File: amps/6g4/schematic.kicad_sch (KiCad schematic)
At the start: 77 parts, among them T1 8087, T2 45216

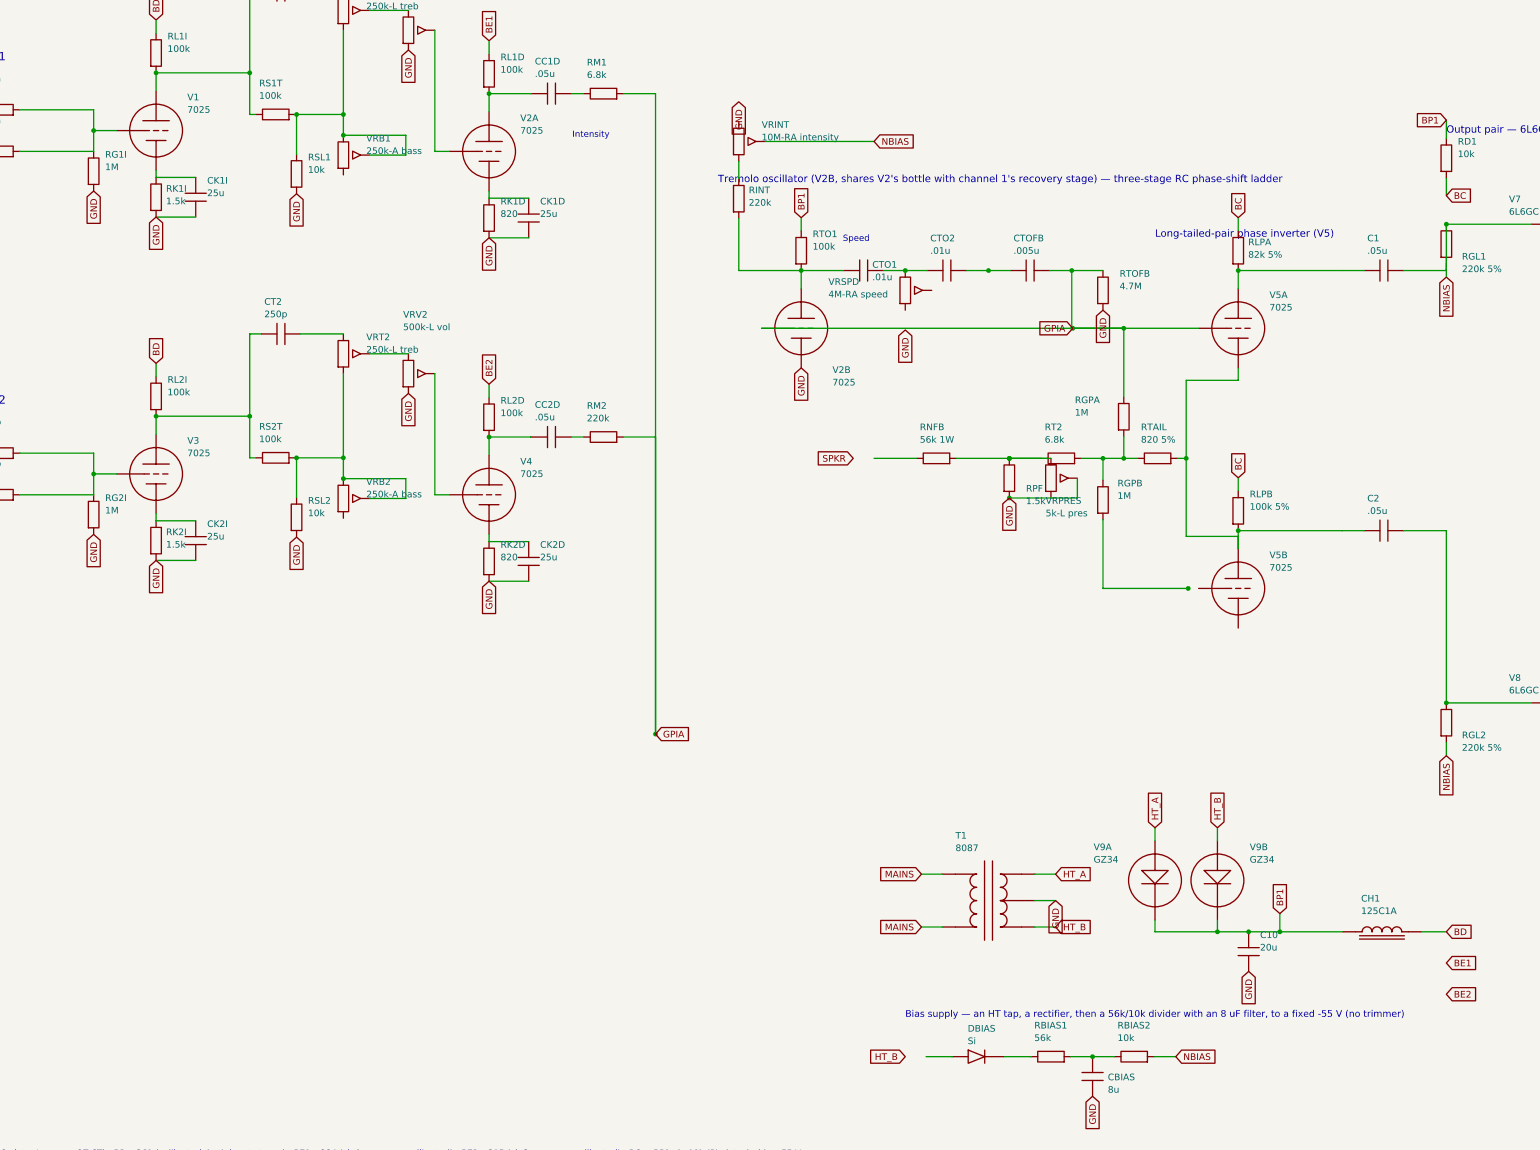
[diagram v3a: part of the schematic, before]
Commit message: Fix: deterministic schematic ids and wires split at every join
- _u() is uuid5 over (amp id, emission order), so a regeneration of an
  unchanged script is byte-identical and a drift gate becomes possible
- write() splits wire segments at symbol pins, wire ends and junction dots,
  so the file connects exactly what the drawing shows under KiCad's
  endpoint-only semantics (270 pins were on a wire's interior; net
  partitions unchanged on all 38 sheets)
- all sheets regenerated; aa864-bassman title block was stale (draft) and
  now matches meta.yaml (verified)

Co-Authored-By: Claude Fable 5.1 <noreply@anthropic.com>
Claude-Session: https://claude.ai/code/session_01KBMfdh37HmCL2iWcBiL5J1
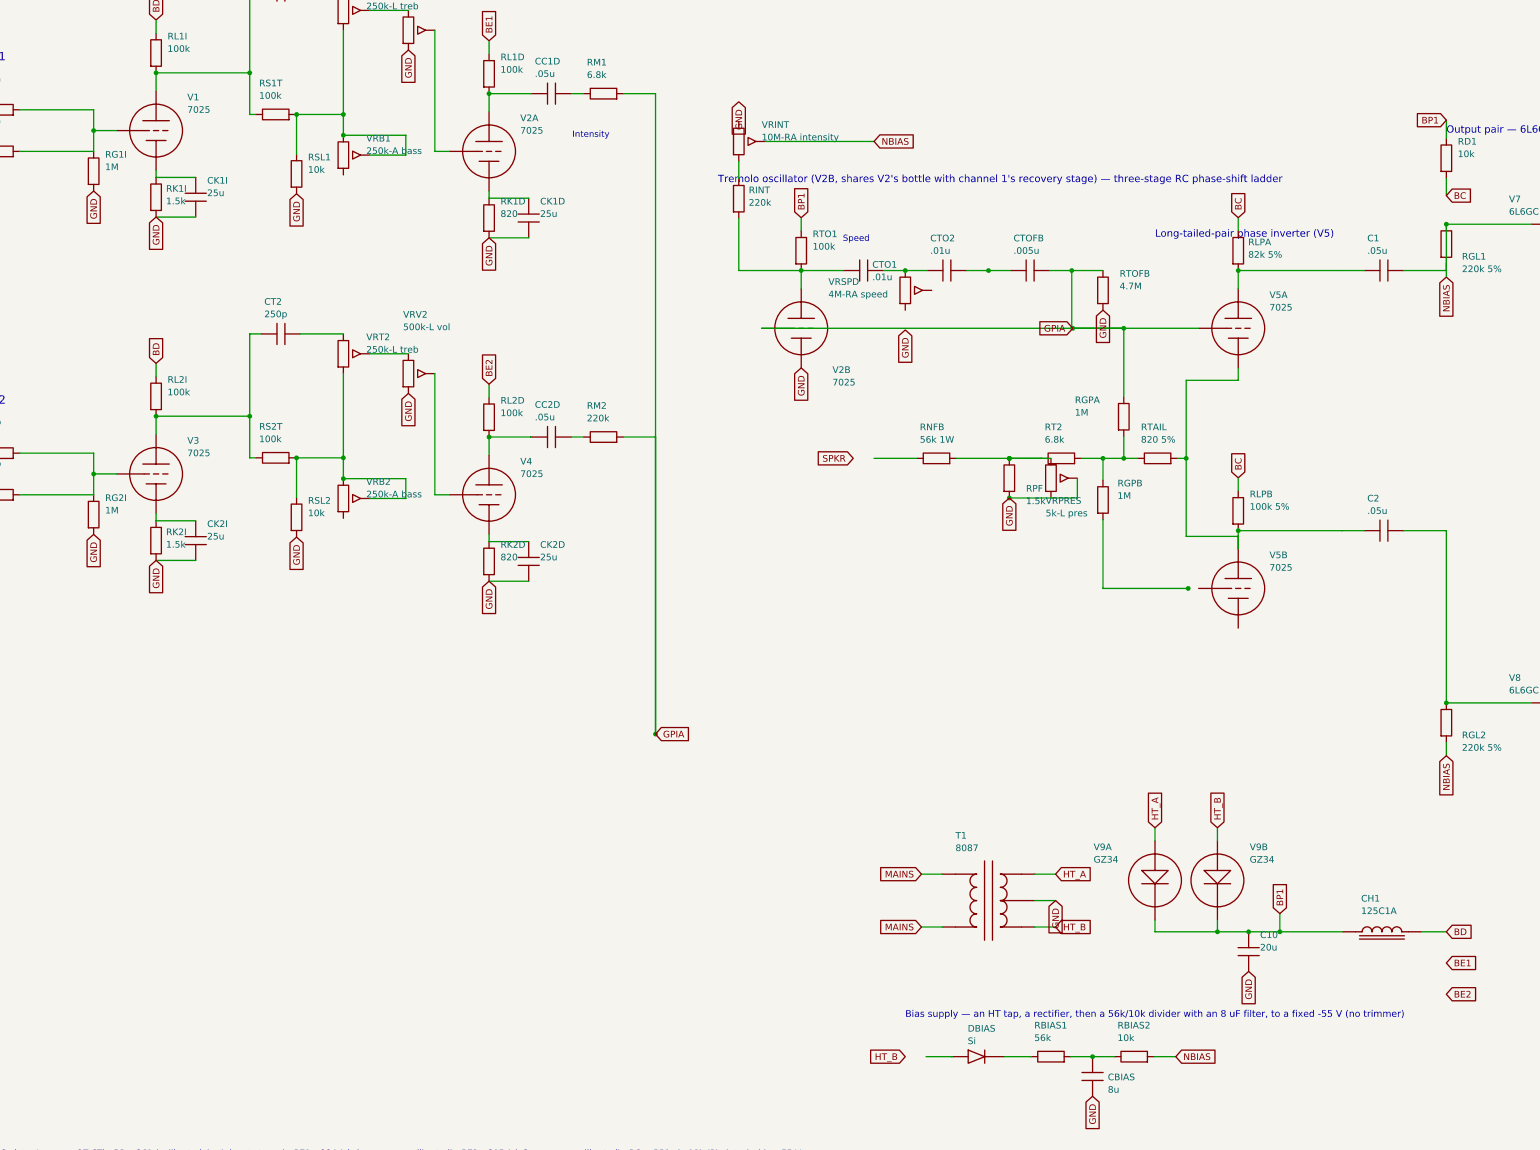
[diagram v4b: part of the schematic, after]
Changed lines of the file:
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@@
   (wire (pts (xy 35.146 50.699) (xy 49.336 50.699))
     (stroke (width 0) (type default)))
-  (wire (pts (xy 49.336 42.699) (xy 49.336 50.699))
+  (wire (pts (xy 49.336 42.699) (xy 49.336 46.699))
+    (stroke (width 0) (type default)))
+  (wire (pts (xy 49.336 46.699) (xy 49.336 50.699))
     (stroke (width 0) (type default)))
   (junction (at 49.336 46.699) (diameter 0) (color 0 0 0 0))
@@
   (wire (pts (xy 151.146 39.599) (xy 157.336 39.599))
     (stroke (width 0) (type default)))
-  (wire (pts (xy 157.336 39.599) (xy 157.336 162.699))
+  (wire (pts (xy 157.336 39.599) (xy 157.336 105.599))
+    (stroke (width 0) (type default)))
+  (wire (pts (xy 157.336 105.599) (xy 157.336 162.699))
     (stroke (width 0) (type default)))
   (text "Channel 2" (at 21.336 98.699 0)
@@
   (wire (pts (xy 35.146 116.699) (xy 49.336 116.699))
     (stroke (width 0) (type default)))
-  (wire (pts (xy 49.336 108.699) (xy 49.336 116.699))
+  (wire (pts (xy 49.336 108.699) (xy 49.336 112.699))
+    (stroke (width 0) (type default)))
+  (wire (pts (xy 49.336 112.699) (xy 49.336 116.699))
     (stroke (width 0) (type default)))
   (junction (at 49.336 112.699) (diameter 0) (color 0 0 0 0))
@@
   (global_label "GPIA" (shape input) (at 237.526 84.699 180)
     (effects (font (size 1.27 1.27)) (justify right)))
-  (wire (pts (xy 237.526 84.699) (xy 261.716 84.699))
+  (wire (pts (xy 237.526 84.699) (xy 247.336 84.699))
+    (stroke (width 0) (type default)))
+  (wire (pts (xy 247.336 84.699) (xy 261.716 84.699))
     (stroke (width 0) (type default)))
   (symbol (lib_id "cx:TRIODE") (at 269.336 84.699 0) (unit 1)
@@
   (global_label "BC" (shape input) (at 269.336 63.439 90)
     (effects (font (size 1.27 1.27)) (justify left)))
-  (wire (pts (xy 269.336 127.079) (xy 269.336 123.599))
+  (wire (pts (xy 269.336 127.079) (xy 269.336 124.699))
+    (stroke (width 0) (type default)))
+  (wire (pts (xy 269.336 124.699) (xy 269.336 123.599))
     (stroke (width 0) (type default)))
   (symbol (lib_id "cx:R") (at 269.336 119.789 0) (unit 1)
@@
   (wire (pts (xy 269.336 124.699) (xy 259.336 124.699))
     (stroke (width 0) (type default)))
-  (wire (pts (xy 259.336 94.699) (xy 259.336 124.699))
+  (wire (pts (xy 259.336 94.699) (xy 259.336 109.699))
+    (stroke (width 0) (type default)))
+  (wire (pts (xy 259.336 109.699) (xy 259.336 124.699))
     (stroke (width 0) (type default)))
   (junction (at 259.336 109.699) (diameter 0) (color 0 0 0 0))
@@
     (property "Reference" "RT2" (at 232.136 103.699 270) (effects (font (size 1.27 1.27)) (justify left)))
     (property "Value" "6.8k" (at 232.136 106.099 270) (effects (font (size 1.27 1.27)) (justify left))))
-  (wire (pts (xy 239.146 109.699) (xy 247.336 109.699))
+  (wire (pts (xy 239.146 109.699) (xy 243.336 109.699))
+    (stroke (width 0) (type default)))
+  (wire (pts (xy 243.336 109.699) (xy 247.336 109.699))
     (stroke (width 0) (type default)))
   (wire (pts (xy 231.526 109.699) (xy 225.336 109.699))
@@
     (property "Reference" "VRPRES" (at 232.32 117.849 0) (effects (font (size 1.27 1.27)) (justify left)))
     (property "Value" "5k-L pres" (at 232.32 120.249 0) (effects (font (size 1.27 1.27)) (justify left))))
-  (wire (pts (xy 233.336 109.699) (xy 225.336 109.699))
+  (wire (pts (xy 233.336 109.699) (xy 231.526 109.699))
+    (stroke (width 0) (type default)))
+  (wire (pts (xy 231.526 109.699) (xy 225.336 109.699))
     (stroke (width 0) (type default)))
   (junction (at 225.336 109.699) (diameter 0) (color 0 0 0 0))
@@
   (wire (pts (xy 301.146 73.599) (xy 309.336 73.599))
     (stroke (width 0) (type default)))
-  (wire (pts (xy 309.336 73.599) (xy 309.336 64.699))
+  (wire (pts (xy 309.336 73.599) (xy 309.336 72.319))
+    (stroke (width 0) (type default)))
+  (wire (pts (xy 309.336 72.319) (xy 309.336 64.699))
     (stroke (width 0) (type default)))
   (symbol (lib_id "cx:C") (at 297.336 123.599 90) (unit 1)
@@
     (property "Reference" "RGL1" (at 312.336 70.909 0) (effects (font (size 1.27 1.27)) (justify left)))
     (property "Value" "220k 5%" (at 312.336 73.309 0) (effects (font (size 1.27 1.27)) (justify left))))
-  (wire (pts (xy 309.336 72.319) (xy 309.336 74.859))
+  (wire (pts (xy 309.336 72.319) (xy 309.336 73.599))
+    (stroke (width 0) (type default)))
+  (wire (pts (xy 309.336 73.599) (xy 309.336 74.859))
     (stroke (width 0) (type default)))
   (global_label "NBIAS" (shape input) (at 309.336 74.859 270)
@@
   (wire (pts (xy 265.336 198.439) (xy 265.336 200.699))
     (stroke (width 0) (type default)))
-  (wire (pts (xy 253.336 200.699) (xy 277.336 200.699))
+  (wire (pts (xy 253.336 200.699) (xy 265.336 200.699))
+    (stroke (width 0) (type default)))
+  (wire (pts (xy 265.336 200.699) (xy 271.336 200.699))
+    (stroke (width 0) (type default)))
+  (wire (pts (xy 271.336 200.699) (xy 277.336 200.699))
     (stroke (width 0) (type default)))
   (junction (at 265.336 200.699) (diameter 0) (color 0 0 0 0))
@@
   (global_label "HT_B" (shape input) (at 205.336 224.699 180)
     (effects (font (size 1.27 1.27)) (justify right)))
-  (wire (pts (xy 209.336 224.699) (xy 214.416 224.699))
+  (wire (pts (xy 209.336 224.699) (xy 214.256 224.699))
+    (stroke (width 0) (type default)))
+  (wire (pts (xy 214.256 224.699) (xy 214.416 224.699))
     (stroke (width 0) (type default)))
   (symbol (lib_id "cx:DIODE_SS") (at 219.336 224.699 0) (unit 1)

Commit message: Fix: schematic wiring on 6g3, 6g4, 6g5, 6g6b
- long-tailed pair tail moved off section B's plate to its cathode (6g3,
  6g4, 6g5); 6g4 V8 plate lead was drawn under its grounded cathode
- 6g6b: all five OT leads on bare coordinates with the secondary drawn on
  the primary side; bias line taken off the bleeder's grounded end (NBIAS
  and GND one net); both tone networks rebuilt; mixing bus ran through
  V3A's bottle
- eight parts shorted end to end, invisible to the pin check: 6g4 RGL1;
  6g5 RG5 (mixing node on ground); 6g6b C11, RG4B, RNFB, RTAIL, RTN1, VR3
- 6g5: treble pot runs off each other's lug, driver run 12 mm short of
  V6A grid, CFB1 rotated but wired upright, choke leads short both ends
- five dated waivers (bridge rectifier centre tap, footswitch terminal
  not lettered on the source, mains side outside the drawing, VR7's
  undesignated cap)
- OPEN, not guessed: 6g5 presence network is drawn as a DC path to ground
  (RPRES + pot in series) while netlist.cir has RT2 to ground and calls the
  network DC-neutral; sources do not settle it — sheet stays unclaimed

Co-Authored-By: Claude Fable 5.1 <noreply@anthropic.com>
Claude-Session: https://claude.ai/code/session_01KBMfdh37HmCL2iWcBiL5J1
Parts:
- removed C1: .05u, symbol cx:C
- removed CTO2: .01u, symbol cx:C
- removed RBIAS1: 56k, symbol cx:R
- removed RGL1, RGL2: 220k 5%, symbol cx:R
- removed RLPA: 82k 5%, symbol cx:R
- removed RT2: 6.8k, symbol cx:R
- removed RTOFB: 4.7M, symbol cx:R
- added C2: .05u, symbol cx:C
- added CBIAS: 8u, symbol cx:C
- added CTOFB: .005u, symbol cx:C
- added RINT: 220k, symbol cx:R
- added RLPB: 100k 5%, symbol cx:R
- added RNFB: 56k 1W, symbol cx:R
- added RS1: 470 1W, symbol cx:R
- added T2: 45216, symbol cx:OT_PP
- CTO2: renamed from CTOFB; value .005u -> .01u
- RBIAS1: renamed from CBIAS; value 8u -> 56k; symbol cx:C -> cx:R
- RGL1: renamed from RS1; value 470 1W -> 220k 5%
- RGL2: renamed from RS2; value 470 1W -> 220k 5%
- RLPA: renamed from RLPB; value 100k 5% -> 82k 5%
- RS2: renamed from T2; value 45216 -> 470 1W; symbol cx:OT_PP -> cx:R
- RT2: renamed from RNFB; value 56k 1W -> 6.8k
- RTOFB: renamed from RINT; value 220k -> 4.7M
- renumbered C2 to C1
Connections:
- net BC: now also RLPB.1
- net BP1: now also RS2.2, RS1.2, T2.2 (CT); no longer RGL1.2, RGL2.2
- net CH1 IN 1: now also R1a.1
- net CH1 IN 2: now also R2a.1
- net CH2 IN 1: now also R1b.1
- net CH2 IN 2: now also R2b.1
- net GND: now also RTOFB.2, VRINT.1, VRSPD.2 (W), VRSPD.3, CBIAS.2, T2.5 (SEC_C); no longer RBIAS1.2, RS2.5 (SEC_C)
- net HT_B: now also DBIAS.1 (A)
- net NBIAS: now also RGL1.2, RGL2.2; no longer V7.2 (G1)
- net SPKR: now also RNFB.1, T2.4 (SEC_H); no longer RS2.4 (SEC_H)
- net at V5A.1 (P): now also C1.1, RLPA.2
- net at CTO2.1: now also CTO1.2, VRSPD.1
- net at CTO2.2: now also CTOFB.1; no longer V2B.2 (G)
- net at RS1T.2, VRB1.1, VRB1.2 (W)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: no longer RSL1.1
- net at VRB1.3: now also RSL1.1
- net at CTO1.1, RTO1.2, V2B.1 (P): now also RINT.2; no longer RTOFB.2
- net at RPF.1, VRPRES.1: now also RT2.1, RNFB.2; no longer RT2.2
- net at RGPA.2, RGPB.1, RTAIL.1: now also RT2.2
- net at RGL1.1: now also C1.2, V7.2 (G1); no longer V7.3 (G2)
- net at RS2T.2, VRB2.1, VRB2.2 (W)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: no longer RSL2.1
- net at DBIAS.2 (K): now also RBIAS1.1
- net at RBIAS2.1: now also RBIAS1.2, CBIAS.1; no longer RBIAS1.1
- net at V8.2 (G1): now also RGL2.1, C2.2; no longer C1.2
- net at VRINT.3: now also RINT.1; no longer RTOFB.1
- net at V7.1 (P): now also T2.1 (PRI_A); no longer RS2.1 (PRI_A)
- net at VRB2.3: now also RSL2.1
- net at V5B.2 (G): now also RGPB.2
- net at V5B.3 (K): now also RTAIL.2, V5A.3 (K)
- net at V8.3 (G2): now also RS2.1; no longer RGL2.1
- net at V8.1 (P): now also T2.3 (PRI_B)
- new net: CTOFB.2, RTOFB.1, V2B.2 (G)
- new net: RS1.1, V7.3 (G2)
- new net: C2.1, RLPB.2, V5B.1 (P)
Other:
- moved on the sheet: C1, CTO2, RGL1, RGL2, RLPA, RT2, RTOFB

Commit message: Fix: AB763 Super and 6G4 corrections read back from the factory sheets
AB763 Super (closes #15, closes #16)

The model omitted the Normal channel's second triode entirely and gave the
Vibrato second stage, mix driver and reverb recovery a cathode resistor each.
The C-FD schematic's boxed [A] and [E] are inter-stage connections: [A] ties
the Normal and Vibrato second stages to ONE 820 / 25u network, [E] ties the mix
driver and reverb recovery to another. Because our model omitted one triode's
current, this page claimed the printed chart was internally impossible at three
cathode nodes. It is not. With XV1B added and the shared nodes joined:

  KA   chart 2.1 V   was 1.5 V (-30.0%)   now 2.2 V (+3.6%)
  KE   chart 2.0 V   was 1.5 V (-27.0%)   now 2.2 V (+8.8%)
  PV2  chart 270 V   was 231 V (-14.4%)   now 277 V (+2.6%)

All 20 gated nodes now pass; the accusation is retracted in notes.md and the
retraction is recorded in meta.yaml as audit trail. This is the fourth time the
corpus has accused a factory sheet and been the one at fault.

The Middle control is 10 kOhm-A, not the 250 kOhm published -- 25x, so the
tone-stack curve was wrong, not just the label. Corrected everywhere including
the lab preset; the blackface mid-scoop returns at 15.6 dB / 419 Hz.

With the Middle pot confirmed, topology.tone_stack moves tb -> fmv: this
chassis carries a fixed bleed on one channel and a real Middle pot on the
other, and filing it as treble/bass contradicted its own parts list. The field
names the Vibrato channel and notes.md documents the mixed case.

6G4

Same presence idiom as the 6G5, read off the A-FJ sheet: a 1500 foot resistor
to ground with the 5K-L pot in series with a .1 cap paralleling it. The cap was
missing from the corpus; added as CPRES, 0.1uF, the 200 V read off the layout
page's own .1-200 lettering rather than defaulted from the notice's 400 V.

RNFB is 10 kOhm, not 56 -- traced end to end onto the OT secondary hot. RD1 is
4700 1W, not 10k: the netlist called t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
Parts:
- removed RBIAS1: 56k, symbol cx:R
- removed RGL1, RGL2: 220k 5%, symbol cx:R
- added CBIAS: 8u, symbol cx:C
- added CPRES: .1u 200V, symbol cx:C
- added RS1: 470 1W, symbol cx:R
- added T2: 45216, symbol cx:OT_PP
- RBIAS1: renamed from CBIAS; value 8u -> 56k; symbol cx:C -> cx:R
- RD1: value 10k -> 4.7k 1W
- RGL1: renamed from RS1; value 470 1W -> 220k 5%
- RGL2: renamed from RS2; value 470 1W -> 220k 5%
- RNFB: value 56k 1W -> 10k
- RS2: renamed from T2; value 45216 -> 470 1W; symbol cx:OT_PP -> cx:R
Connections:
- net BP1: now also RS1.2, T2.2 (CT); no longer RGL1.2, RGL2.2
- net GND: now also CBIAS.2, CPRES.2, T2.5 (SEC_C); no longer RBIAS1.2, RS2.5 (SEC_C), VRPRES.2 (W), VRPRES.3
- net NBIAS: now also RGL1.2, RGL2.2
- net SPKR: now also T2.4 (SEC_H); no longer RS2.4 (SEC_H)
- net at RNFB.2, RPF.1, RT2.1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: now also VRPRES.2 (W)
- net at C1.2, V7.2 (G1): now also RGL1.1
- net at V7.1 (P): now also T2.1 (PRI_A); no longer RS2.1 (PRI_A)
- net at V7.3 (G2): now also RS1.1; no longer RGL1.1
- net at RBIAS1.1: now also DBIAS.2 (K); no longer RBIAS2.1
- net at RGL2.1: now also C2.2, V8.2 (G1); no longer V8.3 (G2)
- net at V8.1 (P): now also T2.3 (PRI_B); no longer RS2.3 (PRI_B)
- new net: CPRES.1, VRPRES.3
- new net: RS2.1, V8.3 (G2)
- new net: CBIAS.1, RBIAS1.2, RBIAS2.1
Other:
- note added: "1"
- note added: "2"
- note added: "3"
- note added: "4"
- note added: "5"
- note added: "6"
- note added: "7"
- note added: "8"
- note added: "Rails: BP1 +456 (6L6GC plates/screens, OT CT) · BD +261 (calibrated, both input stages) · BE1 +284 (ch.1 recovery, calibrated) · BE2 +215 (ch.2 recovery, calibrated) · BC = BP1 via 4700 1W (PI plates) · bias -55 V"
- note added: "The phase inverter runs off the BC rail — BP1 through the drawing's own 4700 1W dropper, RD1."
- note removed: "Rails: BP1 +456 (6L6GC plates/screens, OT CT) · BD +261 (calibrated, both input stages) · BE1 +284 (ch.1 recovery, calibrated) · BE2 +215 (ch.2 recovery, calibrated) · BC = BP1 via 10k (PI plates) · bias -55 V"
- note removed: "The phase inverter runs off the BC rail — BP1 through the drawing's own 10k dropper, RD1."
- moved on the sheet: RGL1, RGL2
